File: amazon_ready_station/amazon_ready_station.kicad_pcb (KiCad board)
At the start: 2 copper layers, 35.1 x 65.2 mm, 36 parts, among them J7 BRKOUT_LEFT, J8 BRKOUT_RIGHT, Q1 2N2219, Q2 2N2219

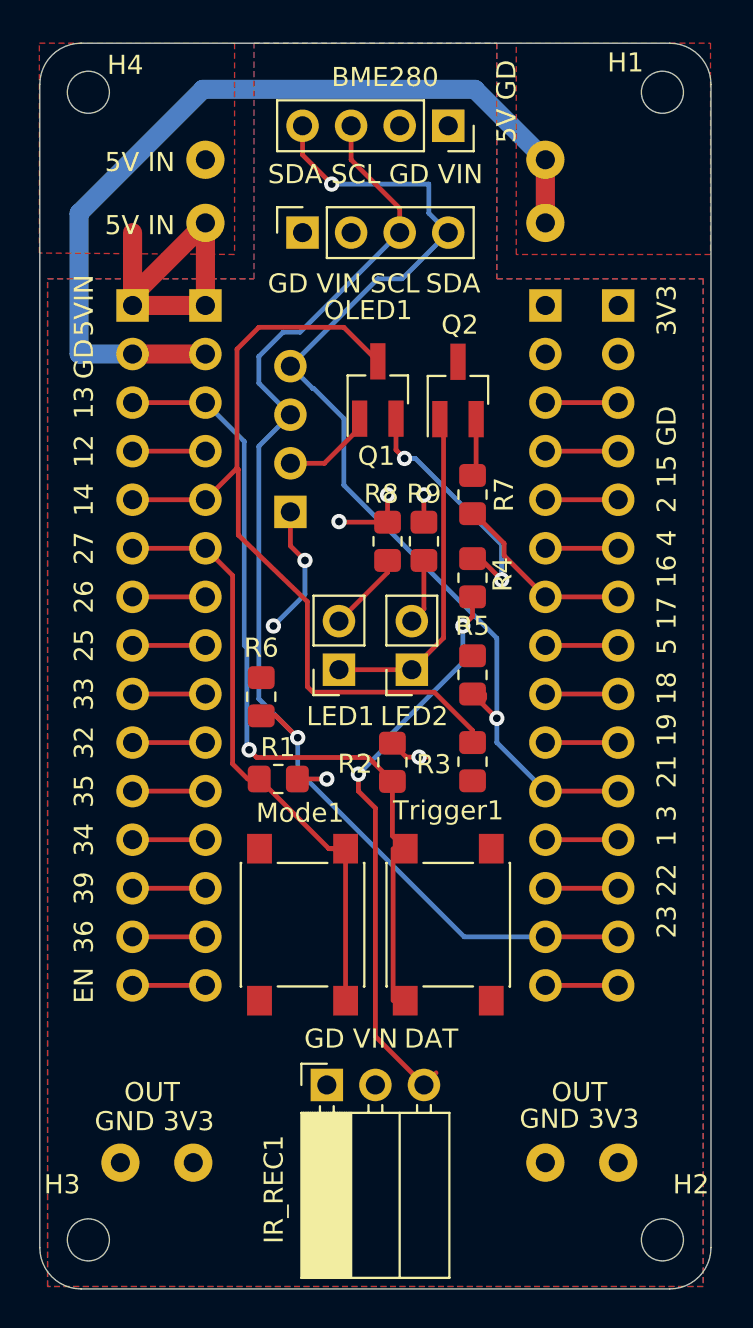
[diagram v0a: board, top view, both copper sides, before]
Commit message: moved LED to bottom, added IR Rec circuit on board
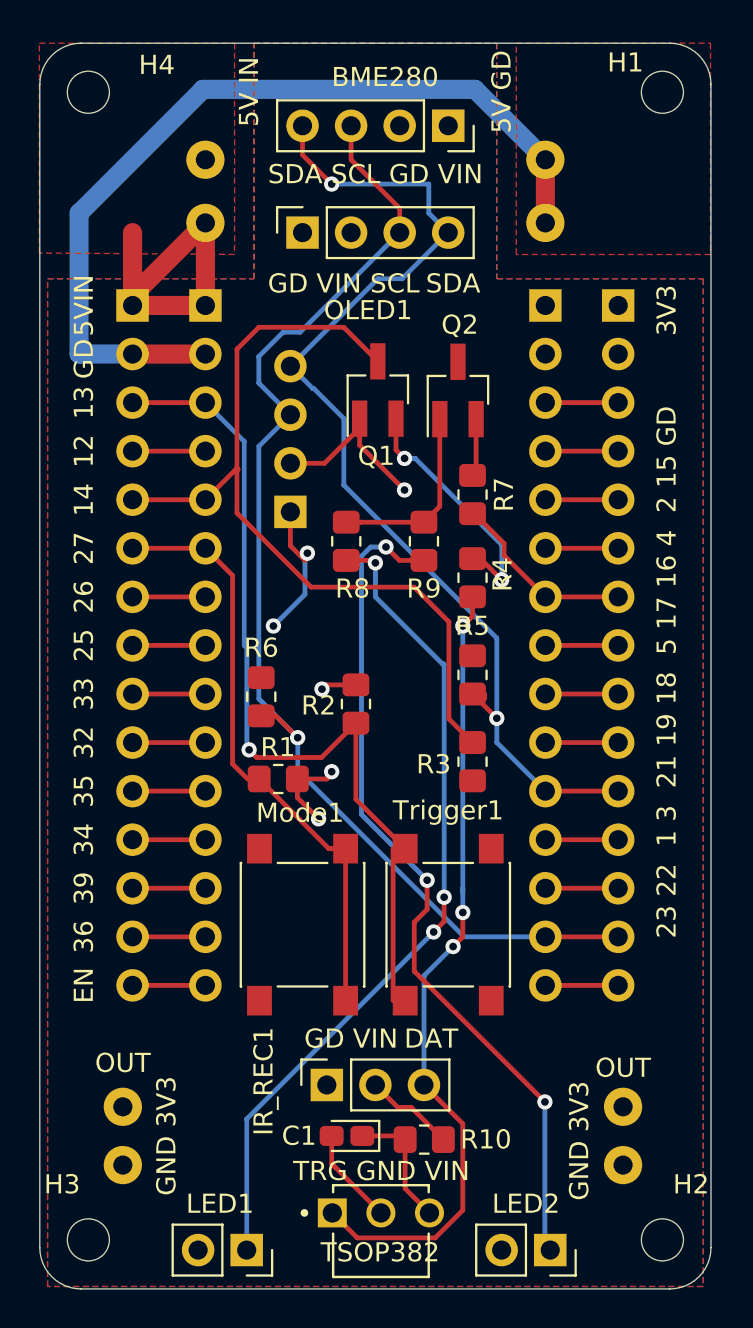
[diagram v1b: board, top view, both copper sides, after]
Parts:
- added C1: 1u, Capacitor_Tantalum_SMD:CP_EIA-1608-08_AVX-J_Pad1.25x1.05mm_HandSolder, F.Cu at (168.7, 160.3)
- added R10: 200, Resistor_SMD:R_0805_2012Metric_Pad1.20x1.40mm_HandSolder, F.Cu at (172.7, 160.5)
- added TSOP382: 1 2 3, TSOP38238:XDCR_TSOP38238, F.Cu at (170.5, 164.3)
- IR_REC1: footprint Connector_PinSocket_2.54mm:PinSocket_1x03_P2.54mm_Horizontal -> Connector_PinSocket_2.54mm:PinSocket_1x03_P2.54mm_Vertical
- moved LED2 31.2 mm to (179.3, 166.2), turned to 270 degrees
- moved LED1 30.7 mm to (163.4, 166.2), turned to 270 degrees
- moved G*** 11.5 mm to (170.1, 134.0)
- moved 3.3V2 4.70 mm to (157.0, 158.8)
- moved GND1 4.07 mm to (183.1, 161.8)
- moved R2 3.59 mm to (169.2, 137.7)
- moved 3.3V1 2.93 mm to (183.1, 158.8)
- moved R8 2.16 mm to (168.7, 129.2), turned to 270 degrees
- moved GND2 0.18 mm to (157.0, 161.8)
- turned R9 to 270 degrees
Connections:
- LED1 pad 2: Net-(LED1-Pad2) -> /GND
- LED2 pad 1: Net-(LED1-Pad1) -> Net-(LED2-Pad1)
- LED2 pad 2: Net-(LED2-Pad2) -> /GND
- Q2 pad 1: Net-(LED1-Pad1) -> Net-(Q2-Pad1)
- R8 pad 1: Net-(LED1-Pad2) -> Net-(Q2-Pad1)
- R8 pad 2: /GND -> Net-(LED1-Pad1)
- R9 pad 1: Net-(LED2-Pad2) -> Net-(Q2-Pad1)
- R9 pad 2: /GND -> Net-(LED2-Pad1)
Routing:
- net Net-(LED2-Pad1): track 0.00 -> 44.7 mm, vias 0 -> 3
- net Net-(LED1-Pad1): track 17.7 -> 43.3 mm, vias 0 -> 3
- net Net-(IR_REC1-Pad3): track 30.9 -> 42.7 mm, vias 2 -> 3
- net Net-(Q2-Pad1): track 0.00 -> 10.1 mm
- net /GND: track 13.7 -> 21.2 mm, vias 5 -> 4
- net Net-(C1-Pad1): track 0.00 -> 6.68 mm
- net /3V3: track 6.98 -> 12.2 mm
- net Net-(LED1-Pad2): track 4.23 -> 0.00 mm
- net Net-(LED2-Pad2): track 3.44 -> 0.00 mm
- net Net-(ESP1-Pad3): track 43.1 -> 46.1 mm
- net Net-(ESP1-Pad5): track 44.2 -> 43.7 mm
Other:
- board text added: "Remote Data Logger v1.8"
- board text added: "TRG GND VIN"
- board text removed: "Remote Data Logger v1.5"
